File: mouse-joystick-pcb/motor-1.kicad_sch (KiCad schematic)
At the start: 28 parts, among them J1 Conn_01x04_P3.5mm_TBH_Horizon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, J2 Conn_01x02_P3.5mm_TBH_Horizon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, J3 Conn_01x05_P3.5mm_TBH_Horizon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, U1 TMC5130A-TA, U2 MAX6816, U5 Logic_LevelTranslator_LSF0102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, X1 16MHz_3.3V

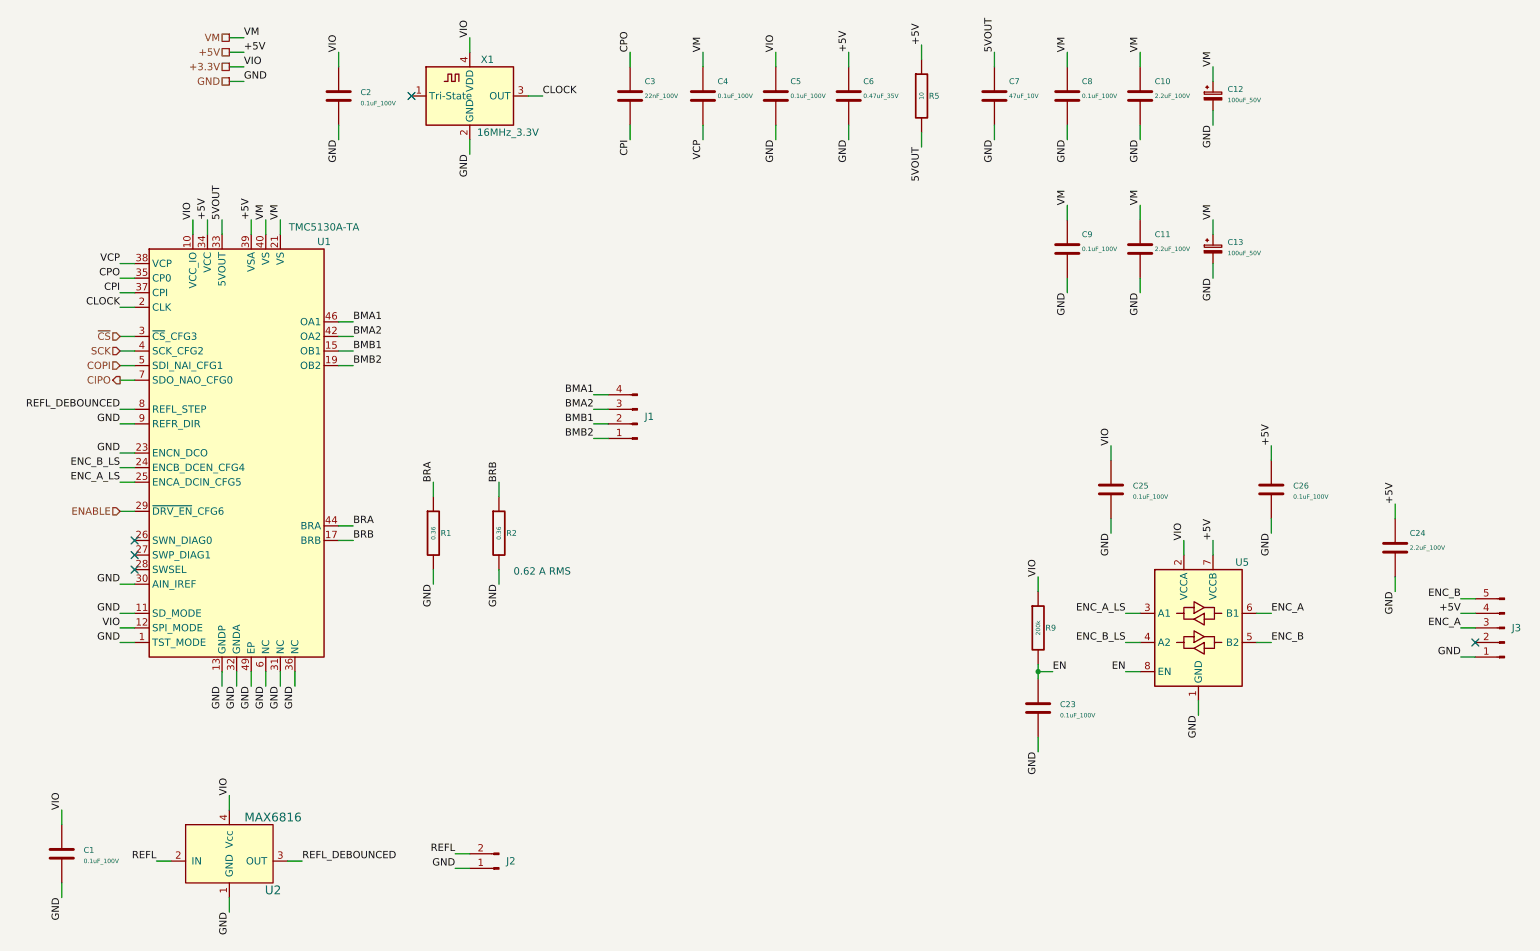
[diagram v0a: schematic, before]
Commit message: Update motor schematics
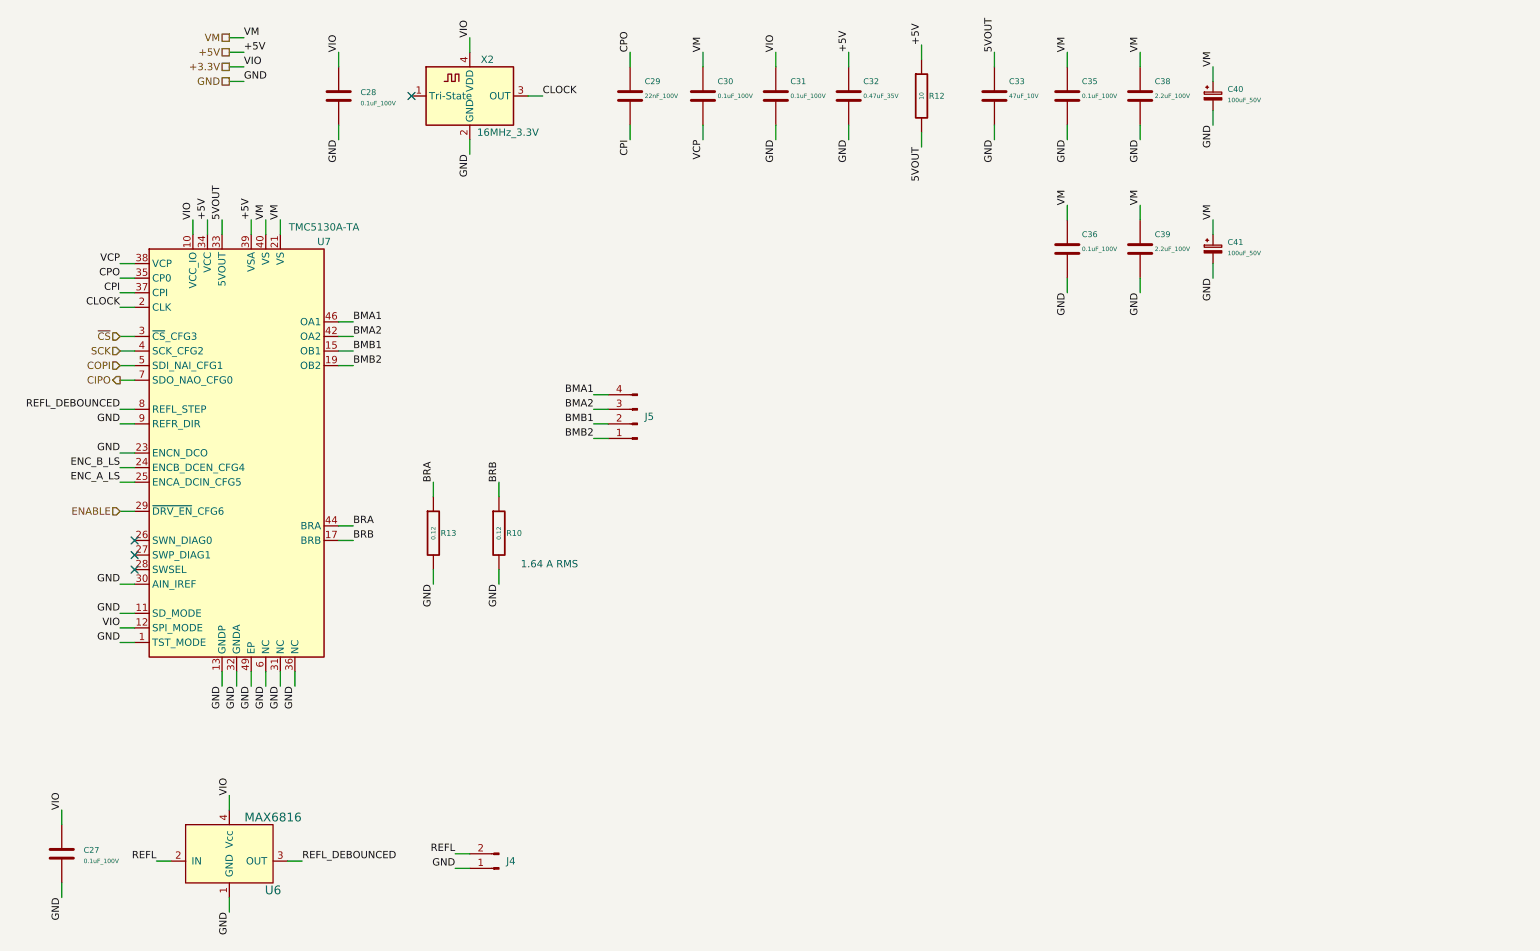
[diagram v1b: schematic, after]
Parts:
- removed C23, C25, C26: 0.1uF_100V, Janelia:C_0402_1005Metric, symbol Janelia:C_0.1uF_100V_0402
- removed C24: 2.2uF_100V, Janelia:C_0805_2012Metric, symbol Janelia:C_2.2uF_100V_0805
- removed J3: Conn_01x05_P3.5mm_TBH_Horizontal_Screw, Janelia:PhoenixContact_MC_1,5_5-G-3.5_1x05_P3.50mm_Horizontal_Screw, symbol Janelia:Conn_01x05_P3.5mm_TBH_Horizontal_Screw
- removed R1, R2: 0.36, Janelia:R_1206_3216Metric, symbol Janelia:R_0.36_250mW_1206_CS
- removed R9: 200k, Janelia:R_0402_1005Metric, symbol Janelia:R_200k_0402
- removed U5: Logic_LevelTranslator_LSF0102DCUR, Janelia:SOP50P310X90-8N, symbol Janelia:Logic_LevelTranslator_LSF0102DCUR
- added R10, R13: 0.12, Janelia:R_1206_3216Metric, symbol Janelia:R_0.12_750mW_1206_CS
- renumbered C1 to C27, C2 to C28, C3 to C29, C4 to C30, C5 to C31, C6 to C32, C7 to C33, C8 to C35, C9 to C36, C10 to C38, C11 to C39, C12 to C40, C13 to C41, J2 to J4, J1 to J5, R5 to R12, U2 to U6, U1 to U7, X1 to X2
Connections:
- net BRA: now also R13.1
- net BRB: now also R10.1
- net GND: now also R10.2, R13.2
- no-connect marks 5 -> 4
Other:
- note added: "1.64 A RMS"
- note removed: "0.62 A RMS"

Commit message: Adjust schmatic
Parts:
- renumbered C27 to C701, C28 to C702, C29 to C703, C30 to C704, C31 to C705, C32 to C706, C33 to C707, C35 to C708, C36 to C709, C38 to C710, C39 to C711, C40 to C712, C41 to C713, J4 to J701, J5 to J702, R13 to R701, R10 to R702, R12 to R703, U6 to U701, U7 to U702, X2 to X701

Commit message: Start wiring schematics
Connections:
- net ENC_A_LS is gone; now on net GND: U702.25 (ENCA_DCIN_CFG5)
- net ENC_B_LS is gone; now on net GND: U702.24 (ENCB_DCEN_CFG4)
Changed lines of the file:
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@@
     (effects (font (size 1.27 1.27)) (justify left bottom))
-  )
-  (label "ENC_A_LS" (at 34.29 111.76 180) (fields_autoplaced)
-    (effects (font (size 1.27 1.27)) (justify right bottom))
   )
   (label "GND" (at 186.69 52.07 270) (fields_autoplaced)
@@
   )
   (label "REFL" (at 40.64 177.8 180) (fields_autoplaced)
+    (effects (font (size 1.27 1.27)) (justify right bottom))
+  )
+  (label "GND" (at 34.29 111.76 180) (fields_autoplaced)
     (effects (font (size 1.27 1.27)) (justify right bottom))
   )
@@
   (label "+5V" (at 55.88 36.83 0) (fields_autoplaced)
     (effects (font (size 1.27 1.27)) (justify left bottom))
+  )
+  (label "GND" (at 34.29 109.22 180) (fields_autoplaced)
+    (effects (font (size 1.27 1.27)) (justify right bottom))
   )
   (label "BRB" (at 74.93 121.92 0) (fields_autoplaced)
@@
     (effects (font (size 1.27 1.27)) (justify left bottom))
   )
-  (label "ENC_B_LS" (at 34.29 109.22 180) (fields_autoplaced)
-    (effects (font (size 1.27 1.27)) (justify right bottom))
-  )
   (label "VIO" (at 55.88 39.37 0) (fields_autoplaced)

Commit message: Finish v1.0 schematic
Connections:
- net ENABLE is gone; now on net GND: U702.29 (~{DRV_EN}_CFG6)
- net DIAG0: now reaches U702.26 (SWN_DIAG0)
- net +3.3V renamed VIO
- no-connect marks 4 -> 3
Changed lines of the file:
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@@
   (title_block
     (title "mouse-joystick-pcb")
-    (date "2024-10-07")
+    (date "2024-10-08")
     (rev "1.0")
     (company "Peter Polidoro")
   )
   (no_connect (at 85.09 44.45))
-  (no_connect (at 36.83 121.92))
   (no_connect (at 36.83 124.46))
   (no_connect (at 36.83 127))
@@
     (stroke (width 0) (type default))
   )
+  (wire (pts (xy 36.83 121.92) (xy 34.29 121.92))
+    (stroke (width 0) (type default))
+  )
   (wire (pts (xy 36.83 76.2) (xy 34.29 76.2))
     (stroke (width 0) (type default))
@@
     (effects (font (size 1.27 1.27)) (justify right bottom))
   )
+  (label "GND" (at 34.29 116.84 180) (fields_autoplaced)
+    (effects (font (size 1.27 1.27)) (justify right bottom))
+  )
   (label "GND" (at 199.39 78.74 270) (fields_autoplaced)
     (effects (font (size 1.27 1.27)) (justify right bottom))
@@
     (effects (font (size 1.27 1.27)) (justify right))
   )
+  (hierarchical_label "DIAG0" (shape output) (at 34.29 121.92 180) (fields_autoplaced)
+    (effects (font (size 1.27 1.27)) (justify right))
+  )
   (hierarchical_label "VM" (shape passive) (at 53.34 34.29 180) (fields_autoplaced)
     (effects (font (size 1.27 1.27)) (justify right))
   )
-  (hierarchical_label "ENABLE" (shape input) (at 34.29 116.84 180) (fields_autoplaced)
-    (effects (font (size 1.27 1.27)) (justify right))
-  )
   (hierarchical_label "SCK" (shape input) (at 34.29 88.9 180) (fields_autoplaced)
     (effects (font (size 1.27 1.27)) (justify right))
@@
     (effects (font (size 1.27 1.27)) (justify right))
   )
-  (hierarchical_label "+3.3V" (shape passive) (at 53.34 39.37 180) (fields_autoplaced)
-    (effects (font (size 1.27 1.27)) (justify right))
-  )
+  (hierarchical_label "VIO" (shape passive) (at 53.34 39.37 180) (fields_autoplaced)
+    (effects (font (size 1.27 1.27)) (justify right))
+  )
